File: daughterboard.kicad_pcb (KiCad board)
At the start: 6 copper layers, 49 x 49 mm, 20 parts, among them J3 Conn_01x38, J4 Conn_01x22, J5 Conn_02x11, U1 LFE5U-12F-6BG256C

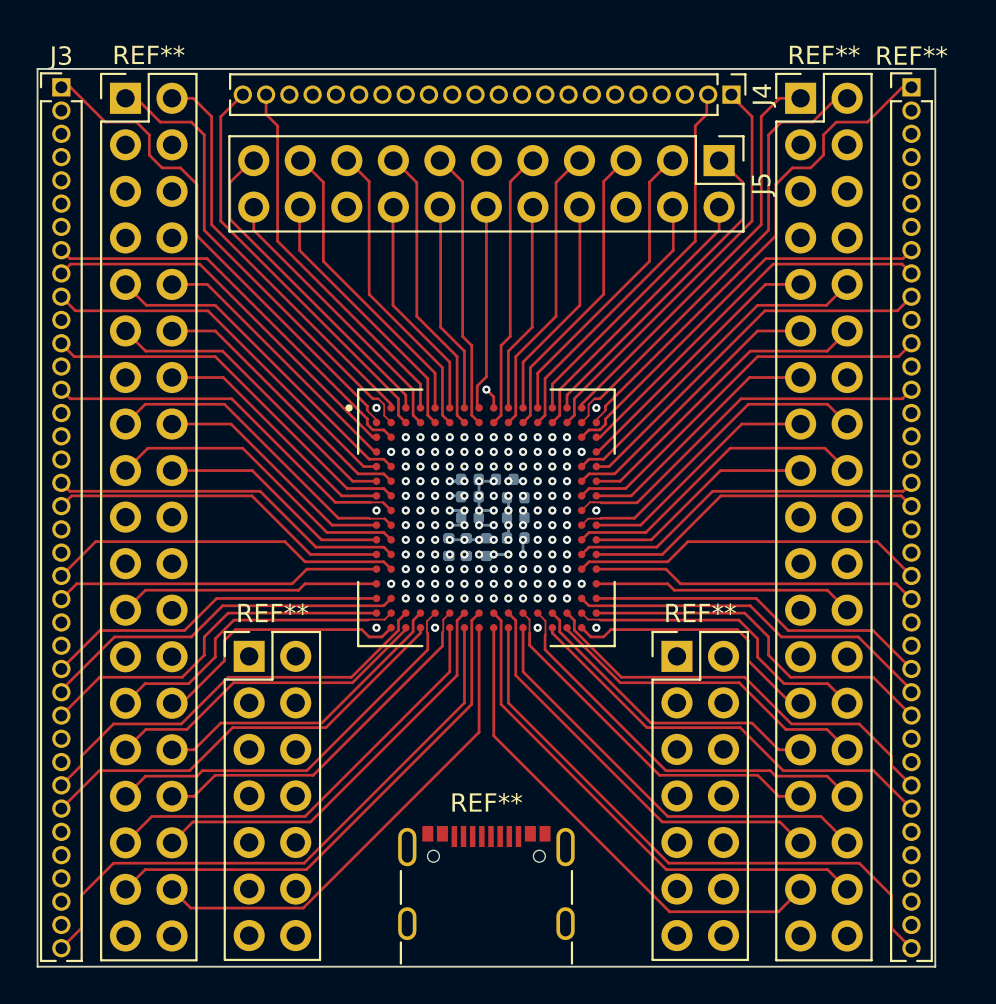
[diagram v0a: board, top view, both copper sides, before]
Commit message: Small routing tweaks, add breakout to schematic
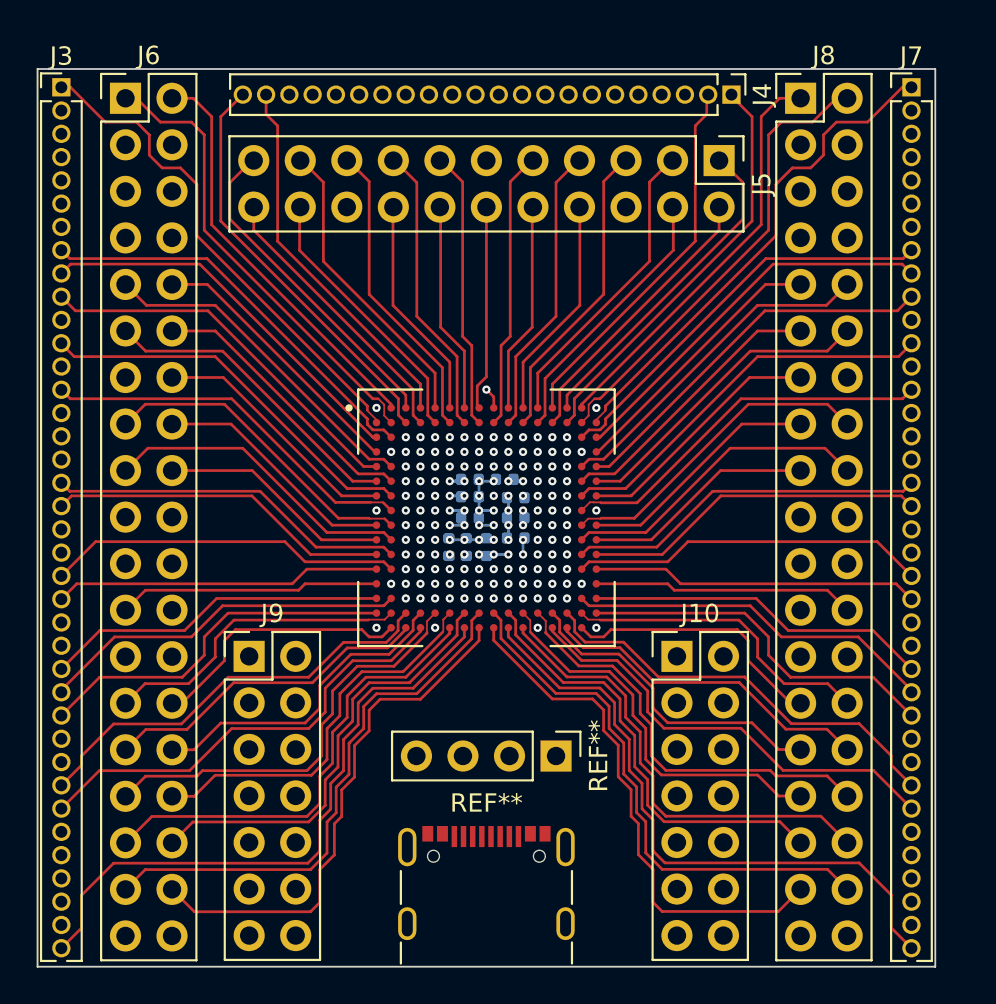
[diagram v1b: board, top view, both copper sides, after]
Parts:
- added REF**: PinHeader_1x04_P2.54mm_Vertical, Connector_PinHeader_2.54mm:PinHeader_1x04_P2.54mm_Vertical, F.Cu at (103.8, 113.0)
- J10, J9: renamed from REF**; value PinHeader_2x07_P2.54mm_Vertical -> Conn_01x14
- J6, J8: renamed from REF**; value PinHeader_2x19_P2.54mm_Vertical -> Conn_01x38
- J7: renamed from REF**; value PinHeader_1x38_P1.27mm_Vertical -> Conn_01x38
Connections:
- net /JTAG/TCK renamed TCK
- net /JTAG/TDI renamed TDI
- net /JTAG/TMS renamed TMS
- net /Programming/PROGRAMN renamed PROGRAMN
- net /Programming/PROG_CLK renamed PROG_CLK
- net /Programming/PROG_DONE renamed PROG_DONE
- net /Programming/PROG_FPGA_CS renamed PROG_FPGA_CS
- J10 pad 10: (no net) -> 5VREGIN
- J10 pad 11: (no net) -> GND
- J10 pad 12: (no net) -> GND
- J10 pad 13: (no net) -> GND
- J10 pad 14: (no net) -> GND
- J10 pad 5: M9 -> CFG1
- J10 pad 6: /JTAG/TDO -> CFG0
- J10 pad 7: (no net) -> GND
- J10 pad 8: (no net) -> GND
- J10 pad 9: (no net) -> 3V3REGIN
- J7 pad 34: CFG0 -> H12
- J7 pad 35: CFG1 -> J12
- J8 pad 37: J12 -> M9
- J8 pad 38: H12 -> TDO
- J9 pad 10: (no net) -> VCCIOB
- J9 pad 11: (no net) -> +2V5
- J9 pad 12: (no net) -> +1V1
- J9 pad 13: (no net) -> GND
- J9 pad 14: (no net) -> GND
- J9 pad 7: (no net) -> 3V3REGOUT
- J9 pad 8: (no net) -> +3V3
- J9 pad 9: (no net) -> VCCIOA
- U1 pad M10: /JTAG/TDO -> TDO
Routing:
- net TDO: track 0.00 -> 33.0 mm, vias 0 -> 1
- net CFG1: track 31.7 -> 13.7 mm
- net /JTAG/TDO: track 17.8 -> 0.00 mm, vias 1 -> 0
- net CFG0: track 31.7 -> 16.8 mm
- net M9: track 16.0 -> 29.1 mm
- net J12: track 32.9 -> 35.8 mm
- net IO0: track 26.9 -> 28.7 mm
- net T9: track 27.1 -> 28.7 mm
- net PROG_FPGA_CS: track 28.2 -> 29.6 mm
- net PROGRAMN: track 28.2 -> 29.6 mm
- net IO1: track 32.7 -> 34.1 mm
- net TCK: track 32.7 -> 34.1 mm
- net T6: track 24.0 -> 25.3 mm
- net TMS: track 24.0 -> 25.3 mm
- net R6: track 20.1 -> 21.4 mm
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
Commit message: Route flash + jtag resistors
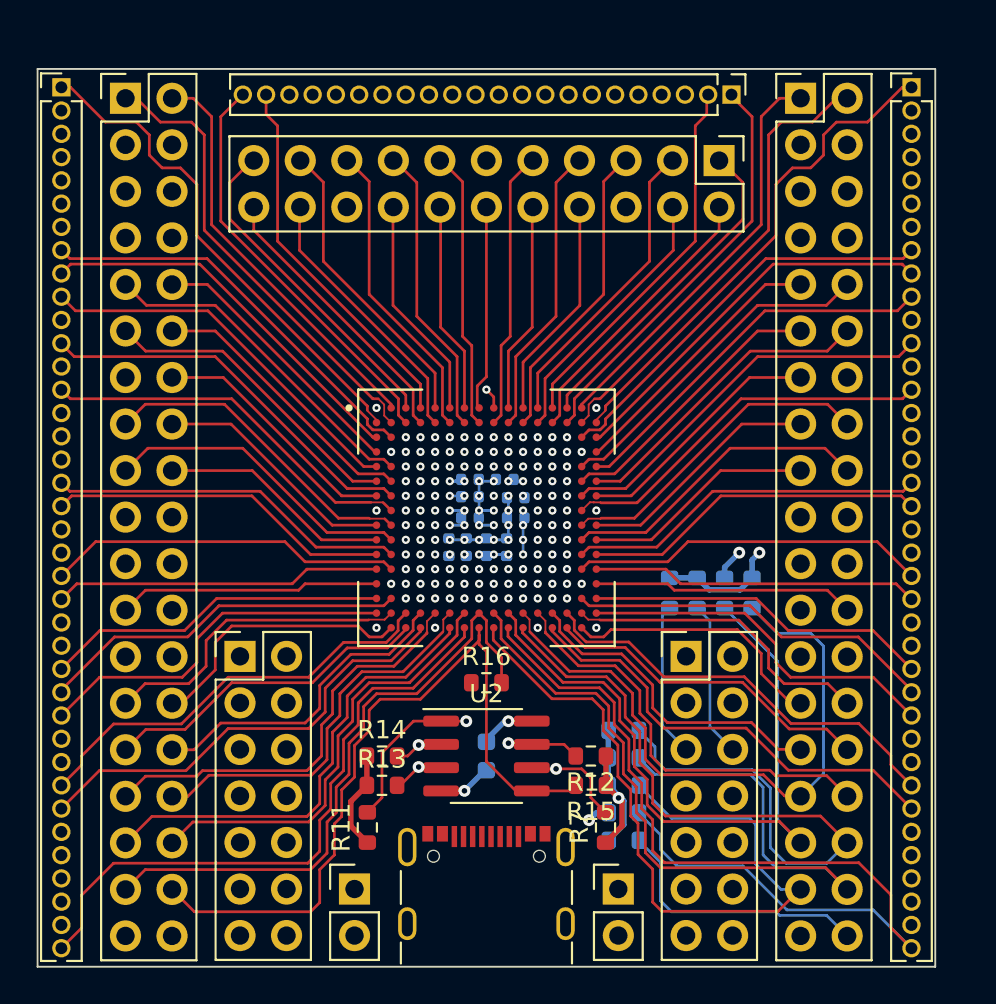
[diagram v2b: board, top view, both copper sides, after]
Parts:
- removed the C12 at (101.6, 101.1)
- removed the REF** at (103.8, 113.0)
- added C4: 0.1 uF, Capacitor_SMD:C_0402_1005Metric, B.Cu at (101.1, 101.6)
- added C9: 10uF, Capacitor_SMD:C_0603_1608Metric, B.Cu at (100.0, 113.0)
- added R1: 4.7K, Resistor_SMD:R_0603_1608Metric, B.Cu at (107.5, 111.6)
- added R10: 4.7K, Resistor_SMD:R_0603_1608Metric, B.Cu at (107.5, 114.6)
- added R11: 4.7K, Resistor_SMD:R_0603_1608Metric, F.Cu at (93.5, 116.9)
- added R12: 10K, Resistor_SMD:R_0603_1608Metric, F.Cu at (105.7, 113.0)
- added R13: 10K, Resistor_SMD:R_0603_1608Metric, F.Cu at (94.3, 114.6)
- added R14: 10K, Resistor_SMD:R_0603_1608Metric, F.Cu at (94.3, 113.0)
- added R15: 10K, Resistor_SMD:R_0603_1608Metric, F.Cu at (105.7, 114.6)
- added R16: 4.7K, Resistor_SMD:R_0603_1608Metric, F.Cu at (100.0, 109.0)
- added R2: 4.7K, Resistor_SMD:R_0603_1608Metric, B.Cu at (107.5, 117.6)
- added R3: 4.7K, Resistor_SMD:R_0603_1608Metric, B.Cu at (114.5, 104.1)
- added R4: 4.7K, Resistor_SMD:R_0603_1608Metric, B.Cu at (107.5, 116.1)
- added R5: 4.7K, Resistor_SMD:R_0603_1608Metric, B.Cu at (111.5, 104.1)
- added R6: 4.7K, Resistor_SMD:R_0603_1608Metric, B.Cu at (110.0, 104.1)
- added R7: 1K, Resistor_SMD:R_0603_1608Metric, F.Cu at (106.5, 116.9)
- added R8: 220, Resistor_SMD:R_0603_1608Metric, B.Cu at (113.0, 104.1)
- added R9: 4.7K, Resistor_SMD:R_0603_1608Metric, B.Cu at (107.5, 113.1)
- added REF**: PinHeader_1x02_P2.54mm_Vertical, Connector_PinHeader_2.54mm:PinHeader_1x02_P2.54mm_Vertical, F.Cu at (107.2, 120.3)
- added REF**: PinHeader_1x02_P2.54mm_Vertical, Connector_PinHeader_2.54mm:PinHeader_1x02_P2.54mm_Vertical, F.Cu at (92.8, 120.3)
- added U2: AT25SF081-SSHD-X, Package_SO:SOIC-8_3.9x4.9mm_P1.27mm, F.Cu at (100.0, 113.0)
- moved J10 0.50 mm to (110.9, 107.6)
- moved J9 0.50 mm to (86.5, 107.6)
- renumbered C9 to C12
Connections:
- C12 pad 1: +3V3 -> +2V8
- U1 pad F6: +3V3 -> +2V8
- U1 pad F7: +3V3 -> +2V8
- U1 pad K11: +2V8 -> +3V3
- U1 pad L11: +2V8 -> +3V3
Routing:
- net PROG_FLASH_CS: track 34.0 -> 76.9 mm, vias 1 -> 2
- net IO3: track 31.7 -> 71.9 mm, vias 1 -> 2
- net PROG_CLK: track 34.0 -> 67.3 mm, vias 1 -> 2
- net +3V3: track 5.93 -> 34.0 mm, vias 9 -> 12
- net IO1: track 34.1 -> 60.9 mm, vias 0 -> 1
- net TCK: track 34.1 -> 52.5 mm
- net TMS: track 25.3 -> 42.5 mm
- net PROGRAMN: track 29.6 -> 46.2 mm
- net TDO: track 33.0 -> 48.2 mm
- net CFG2: track 24.1 -> 38.7 mm
- net TDI: track 21.3 -> 34.9 mm
- net IO2: track 17.8 -> 31.0 mm, vias 1 -> 2
- net IO0: track 28.7 -> 41.4 mm
- net T9: track 28.7 -> 41.2 mm
- net CFG0: track 16.8 -> 25.3 mm
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
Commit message: Route power
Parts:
- added C13: ~, Capacitor_SMD:C_0805_2012Metric, B.Cu at (113.3, 88.7)
- added C14: ~, Capacitor_SMD:C_0805_2012Metric, B.Cu at (109.3, 91.1)
- added C15: ~, Capacitor_SMD:C_0805_2012Metric, B.Cu at (100.3, 90.1)
- added C16: ~, Capacitor_SMD:C_0805_2012Metric, B.Cu at (103.3, 87.2)
- added C17: ~, Capacitor_SMD:C_0805_2012Metric, B.Cu at (90.2, 98.7)
- added C18: ~, Capacitor_SMD:C_0805_2012Metric, B.Cu at (87.3, 95.7)
- added Q1: PMOS, Package_TO_SOT_SMD:SOT-23-3, B.Cu at (112.5, 92.4)
- added Q2: PMOS, Package_TO_SOT_SMD:SOT-23-3, B.Cu at (100.0, 87.2)
- added Q3: NMOS, Package_TO_SOT_SMD:SOT-23-3, B.Cu at (87.3, 99.0)
- added R17: ~, Resistor_SMD:R_0805_2012Metric, B.Cu at (110.0, 87.1)
- added R18: ~, Resistor_SMD:R_0805_2012Metric, B.Cu at (113.3, 86.4)
- added R19: ~, Resistor_SMD:R_0805_2012Metric, B.Cu at (103.3, 90.8)
- added R20: ~, Resistor_SMD:R_0805_2012Metric, B.Cu at (105.4, 87.2)
- added R21: ~, Resistor_SMD:R_0805_2012Metric, B.Cu at (91.0, 95.7)
- added R22: ~, Resistor_SMD:R_0805_2012Metric, B.Cu at (87.3, 93.5)
- added U3: AMS1117-3.3, Package_TO_SOT_SMD:SOT-89-3, B.Cu at (112.5, 97.0)
- added U4: TPS74611PQWDRBRQ1, Package_SON:Texas_S-PVSON-N8, B.Cu at (87.3, 103.5)
- added U5: XC6206P252MR, Package_TO_SOT_SMD:SOT-23-3, B.Cu at (95.4, 87.2)
- C9: footprint Capacitor_SMD:C_0603_1608Metric -> Capacitor_SMD:C_0805_2012Metric
- J1: renamed from REF**; value USB_C_GCT4105 -> USB_C_Receptacle_USB2.0
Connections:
- J1 pad A1: (no net) -> GND
- J1 pad A4: (no net) -> 5VUSB
- J1 pad A5: (no net) -> unconnected-(J1-CC1-PadA5)
- J1 pad A6: (no net) -> unconnected-(J1-D+-PadA6)
- J1 pad A7: (no net) -> unconnected-(J1-D--PadA7)
- J1 pad A8: (no net) -> unconnected-(J1-SBU1-PadA8)
- J1 pad B1: (no net) -> GND
- J1 pad B4: (no net) -> 5VUSB
- J1 pad B5: (no net) -> unconnected-(J1-CC2-PadB5)
- J1 pad B6: (no net) -> unconnected-(J1-D+-PadB6)
- J1 pad B7: (no net) -> unconnected-(J1-D--PadB7)
- J1 pad B8: (no net) -> unconnected-(J1-SBU2-PadB8)
- J1 pad S1: (no net) -> GND
- REF** pad 1: 5VREGIN -> 5VUSB
- REF** pad 2: 5VUSB -> 5VREGIN
- REF** pad 1: 3V3REGIN -> 3V3REGOUT
- REF** pad 2: 3V3REGOUT -> 3V3REGIN
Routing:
- net +2V5: track 0.32 -> 22.8 mm, vias 2 -> 3
- net 5VUSB: track 0.00 -> 13.8 mm
- net Net-(Q1-S): track 0.00 -> 10.3 mm
- net Net-(Q1-G): track 0.00 -> 10.2 mm
- net Net-(Q3-G): track 0.00 -> 7.07 mm
- net Net-(Q2-G): track 0.00 -> 6.97 mm
- net GND: track 21.4 -> 28.2 mm, vias 30 -> 34
- net 1V1REGOUT: track 0.00 -> 6.15 mm
- net 2V5REGOUT: track 0.00 -> 5.82 mm
- net Net-(C14-Pad2): track 0.00 -> 4.67 mm
- net 3V3REGIN: track 0.00 -> 4.11 mm, vias 0 -> 2
- net +1V1: track 3.27 -> 6.90 mm, vias 6 -> 7
- net 3V3REGOUT: track 0.00 -> 2.58 mm, vias 0 -> 1
- net 5VREGIN: track 0.00 -> 2.37 mm, vias 0 -> 1
- net Net-(C18-Pad2): track 0.00 -> 2.22 mm
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- added copper zone on B.Cu, net 1V1REGOUT
- added copper zone on B.Cu, net 2V5REGOUT
- added copper zone on In4.Cu, net 3V3REGIN
- added copper zone on In4.Cu, net 5VREGIN
- added copper zone on B.Cu, net GND
- added copper zone on In3.Cu, net GND

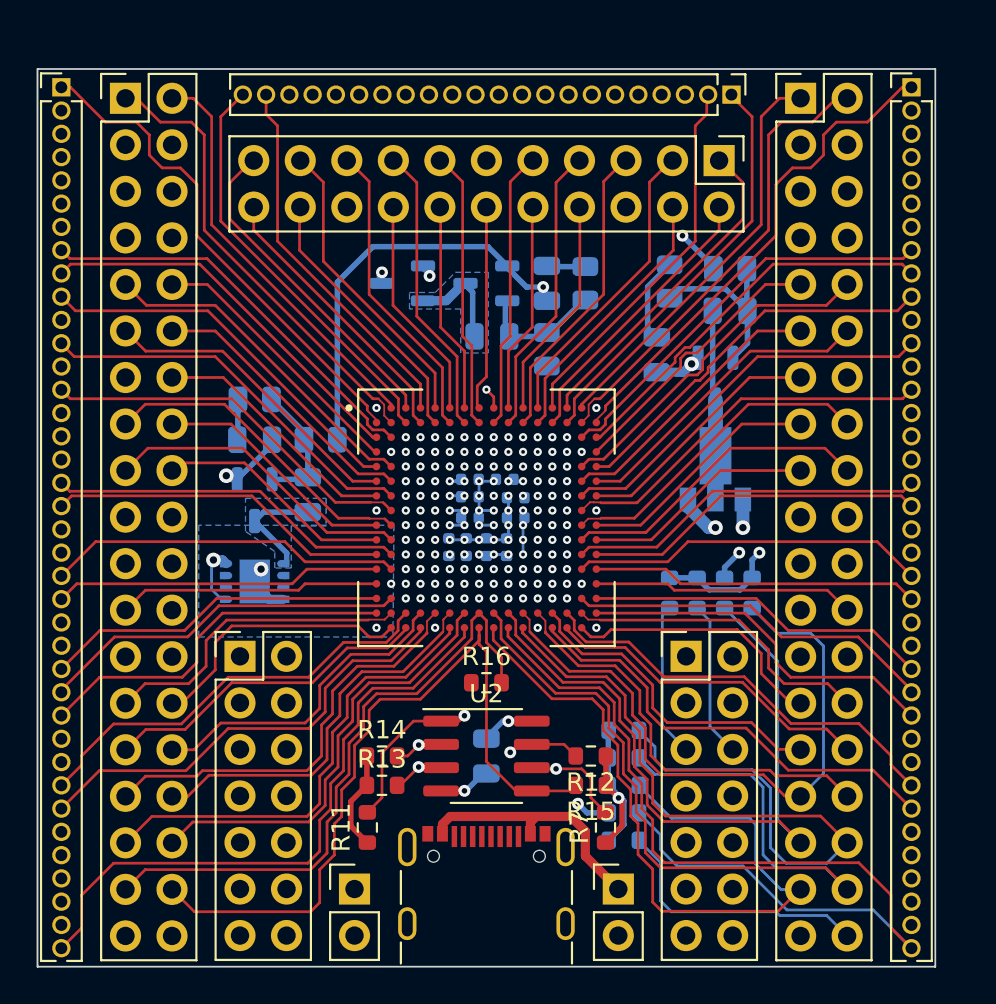
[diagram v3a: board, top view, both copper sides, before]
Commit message: Move programming pins to 100 mil headers
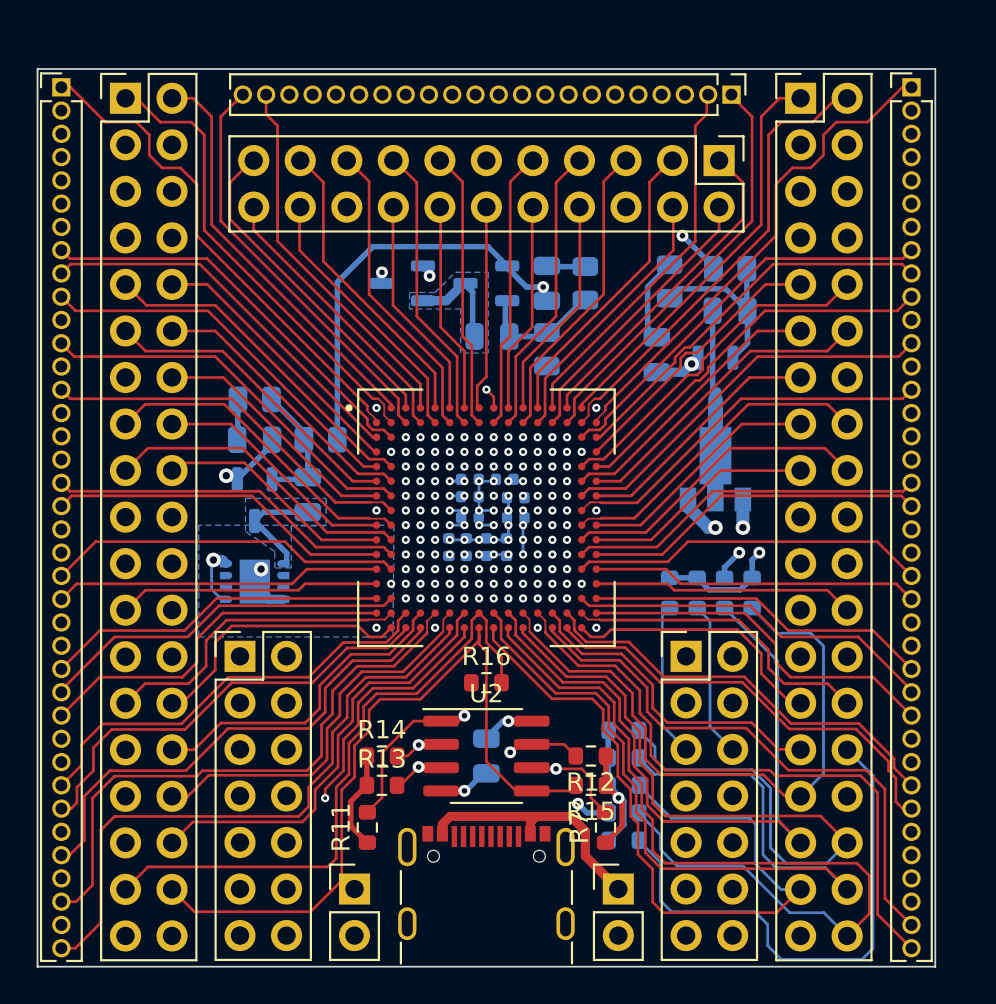
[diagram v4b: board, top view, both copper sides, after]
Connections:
- net T9 renamed nINIT
- J3 pad 32: T4 -> T3
- J3 pad 34: IO3 -> T4
- J3 pad 36: PROG_FLASH_CS -> R5
- J3 pad 38: IO1 -> T6
- J6 pad 29: T3 -> IO1
- J6 pad 31: R5 -> IO3
- J6 pad 33: T6 -> PROG_FLASH_CS
- J7 pad 32: T13 -> T14
- J7 pad 36: PROG_CLK -> M9
- J7 pad 37: PROG_DONE -> T13
- J7 pad 38: TCK -> R12
- J8 pad 30: T14 -> TDO
- J8 pad 32: R12 -> PROG_CLK
- J8 pad 37: M9 -> PROG_DONE
- J8 pad 38: TDO -> TCK
- REF** pad 1: 5VUSB -> (no net)
- REF** pad 2: 5VREGIN -> (no net)
- REF** pad 1: 3V3REGOUT -> (no net)
- REF** pad 2: 3V3REGIN -> (no net)
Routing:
- net PROG_FLASH_CS: track 77.2 -> 39.6 mm
- net IO1: track 60.9 -> 36.9 mm, vias 1 -> 2
- net PROG_CLK: track 67.3 -> 48.8 mm
- net IO3: track 71.5 -> 53.4 mm
- net R12: track 23.2 -> 34.0 mm
- net R5: track 23.2 -> 31.8 mm
- net T6: track 25.3 -> 33.9 mm
- net TDO: track 48.2 -> 55.1 mm
- net J5: track 33.2 -> 39.7 mm
- net T13: track 24.6 -> 30.8 mm
- net T3: track 18.1 -> 24.2 mm
- net T14: track 18.1 -> 24.0 mm
- net TCK: track 52.5 -> 47.6 mm
- net PROG_DONE: track 32.8 -> 27.8 mm
- net H5: track 35.9 -> 40.5 mm
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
